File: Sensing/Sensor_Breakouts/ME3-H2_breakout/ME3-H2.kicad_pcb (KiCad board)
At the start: 2 copper layers, 40.4 x 20.2 mm, 25 parts, among them J1 Conn_01x03_Pin, Q1 PJFET, U1 LT6003HS5TRPBF, U2 LT6003HS5TRPBF, U3 ME3-H2, U4 LM27761

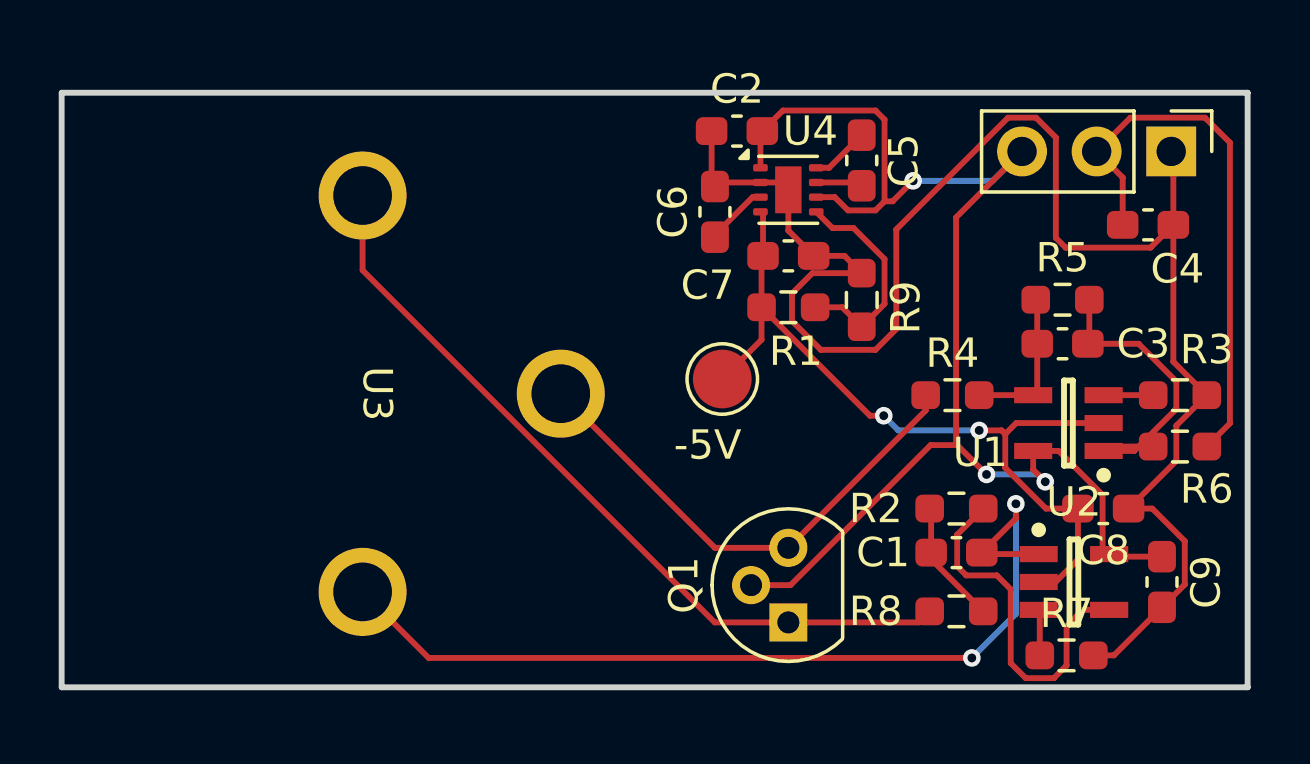
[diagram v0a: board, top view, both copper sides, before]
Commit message: Small Changes to H2 Sensor
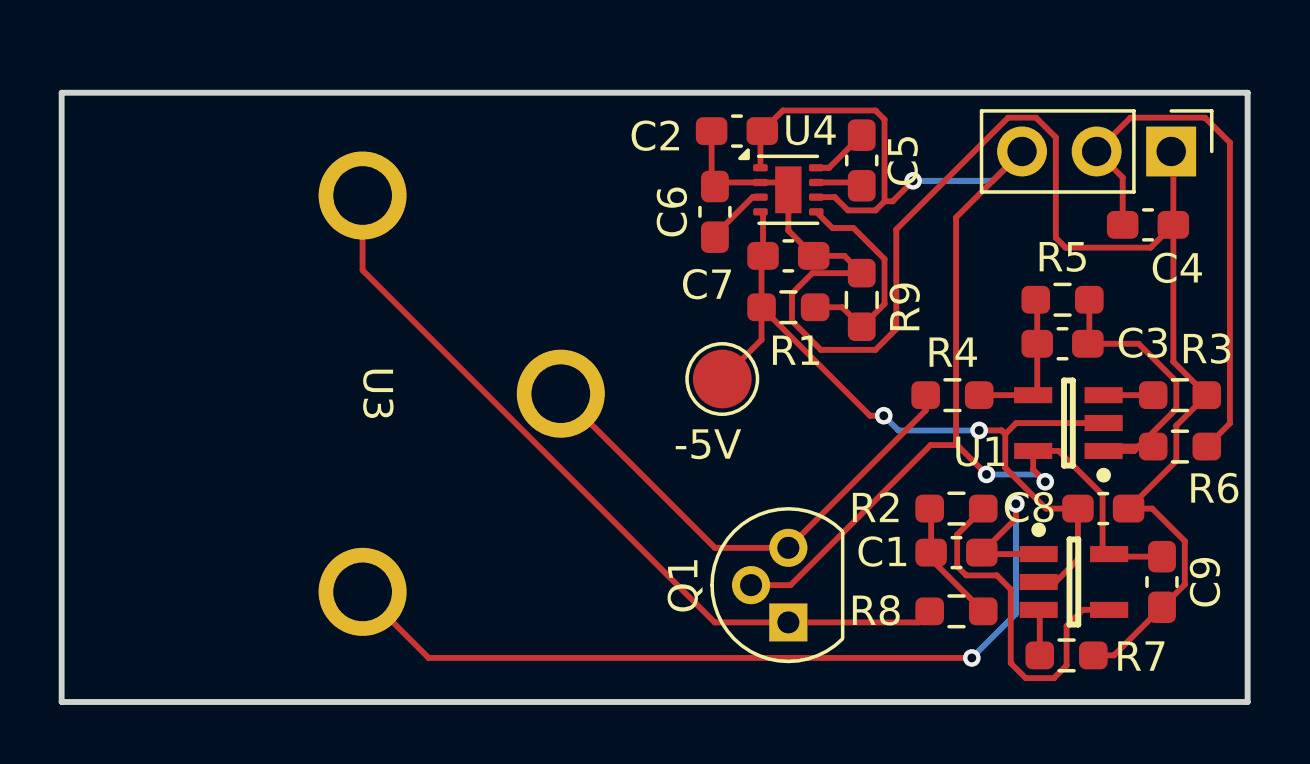
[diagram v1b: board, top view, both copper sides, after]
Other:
- board size 40.4 x 20.2 mm -> 40.4 x 20.8 mm
